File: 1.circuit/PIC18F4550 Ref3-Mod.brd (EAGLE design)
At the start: 91.4 x 55.5 mm, 20 parts, among them J1 PN61729-S, U1 PIC18F4550_40, X1 20Mhz, X2 2540-

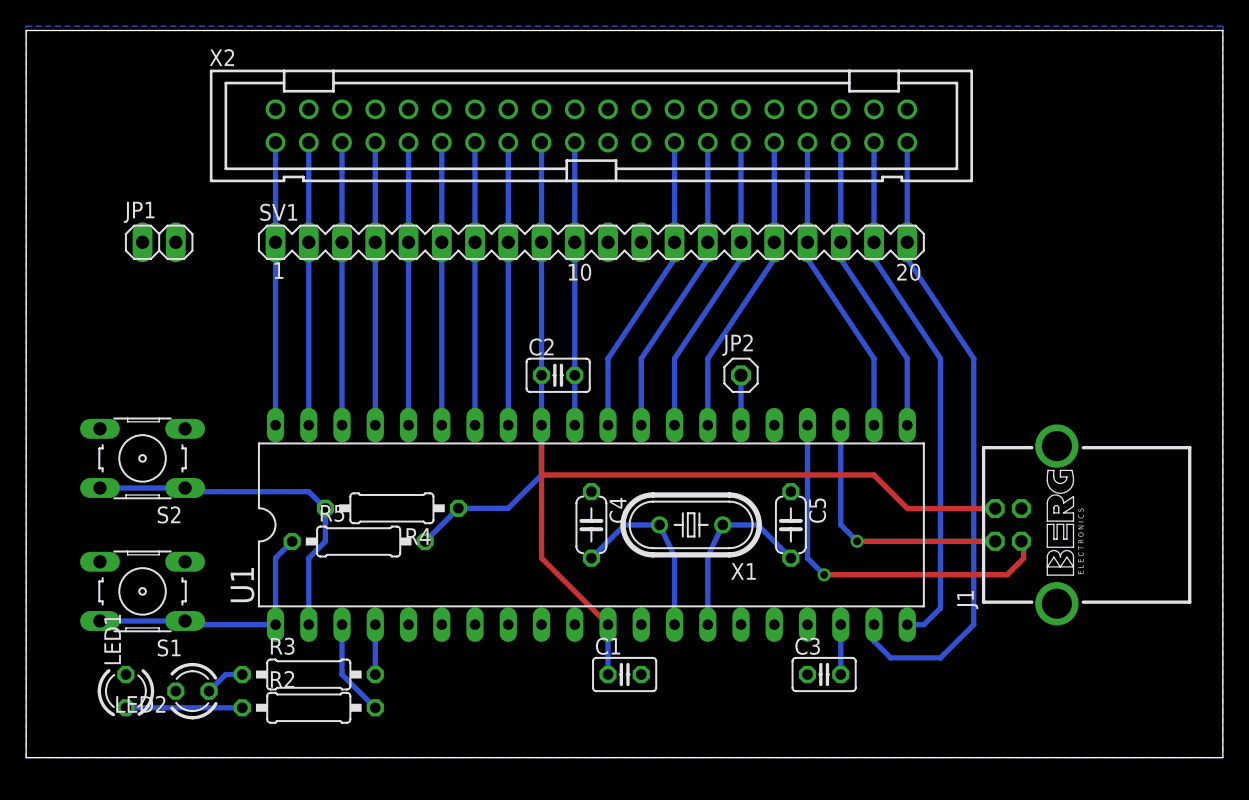
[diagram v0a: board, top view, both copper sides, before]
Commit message: board cleanup of labelling etc, headers added for test probing using scope or logic analyser
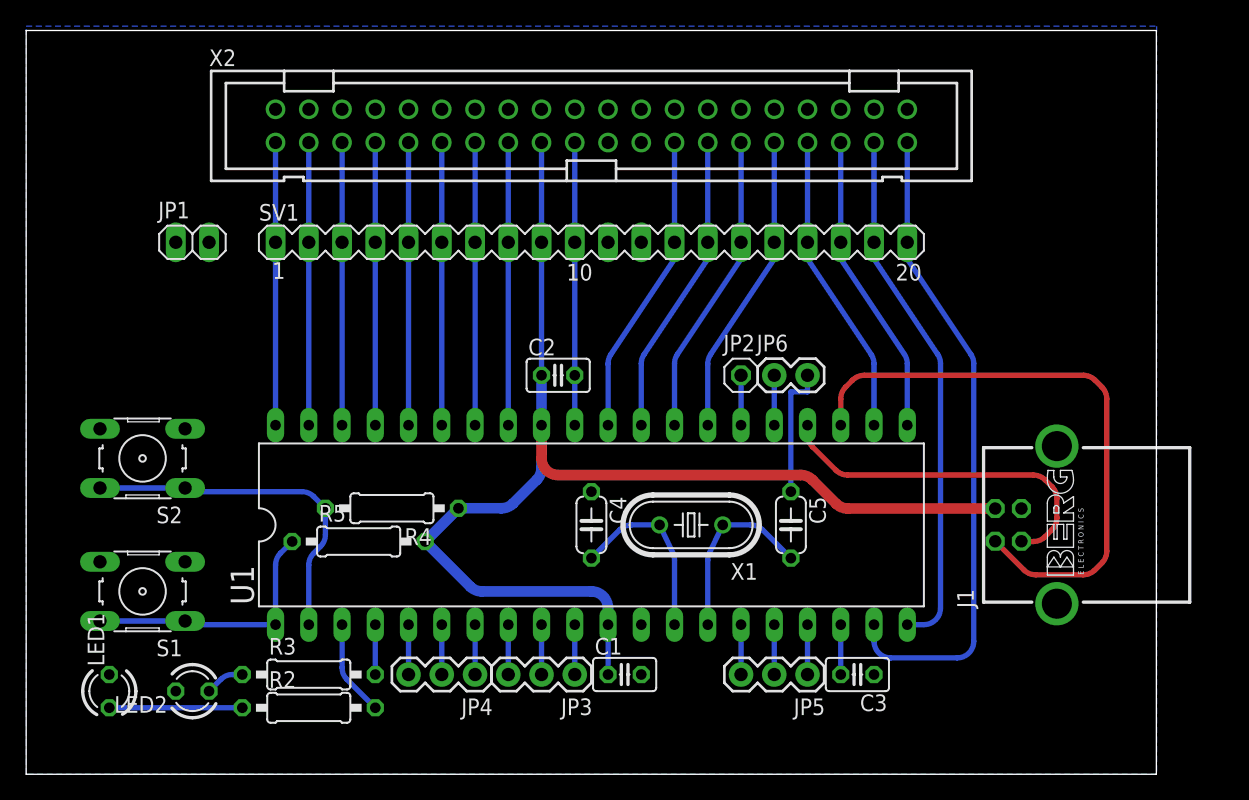
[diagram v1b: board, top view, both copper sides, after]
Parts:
- added JP3, JP4, JP5: (no value), SparkFun:1X03
- added JP6: tx, SparkFun:1X02
- JP1: value scope ground loop -> gnd
- JP2: value (none) -> trig
- LED1: value Ready -> rdy
- LED2: value Attached -> att
- S1: value (none) -> reset
- S2: value (none) -> usr/boot
- moved C3 2.54 mm to (63.5, 6.35), turned to 180 degrees
- moved JP1 2.54 mm to (12.7, 39.4)
- moved LED1 1.27 mm to (6.35, 5.08)
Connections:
- new net N$12: JP3.1, U1.10
- new net N$13: JP3.2, U1.9
- new net N$14: JP3.3, U1.8
- new net N$15: JP4.1, U1.7
- new net N$16: JP4.2, U1.6
- new net N$17: JP4.3, U1.5
- new net N$18: JP5.1, U1.17
- new net N$19: JP5.2, U1.16
- new net N$20: JP5.3, U1.15
- new net TX: JP6.1, U1.25
- net GND: now also JP6.2, X2.10, X2.12, X2.14, X2.16, X2.18, X2.2, X2.20, X2.22, X2.24, X2.26, X2.28, X2.30, X2.32, X2.34, X2.36, X2.38, X2.4, X2.40, X2.6, X2.8
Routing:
- net D-: track 19.9 -> 46.2 mm, vias 1 -> 0
- net GND: track 21.6 -> 31.8 mm
- net TX: track 0.00 -> 3.81 mm
- net N$20: track 0.00 -> 3.81 mm
- net N$19: track 0.00 -> 3.81 mm
- net N$18: track 0.00 -> 3.81 mm
- net N$17: track 0.00 -> 3.81 mm
- net N$16: track 0.00 -> 3.81 mm
- net N$15: track 0.00 -> 3.81 mm
- net N$14: track 0.00 -> 3.81 mm
- net N$13: track 0.00 -> 3.81 mm
- net N$12: track 0.00 -> 3.81 mm
- net +5V: track 93.3 -> 95.9 mm
- net D+: track 29.1 -> 27.2 mm, vias 1 -> 0
- net N$2: track 8.89 -> 10.2 mm
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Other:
- board size 91.4 x 55.5 mm -> 86.3 x 56.8 mm
